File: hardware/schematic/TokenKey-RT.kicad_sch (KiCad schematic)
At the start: 0 parts

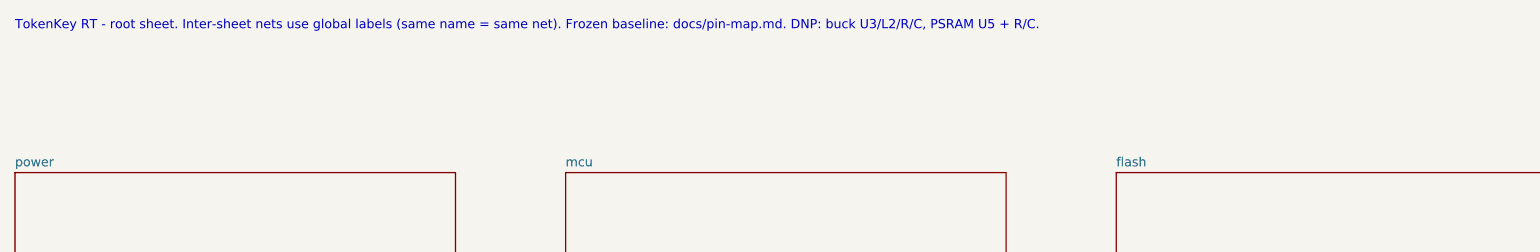
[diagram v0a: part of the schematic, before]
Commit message: PM review fixes: boot R_S, C51, decap note, notes, BOM fields
- MUST: add R22 (R_S) 1k 0402 0402WGF1001TCE / C11702 between Q1 drain
  (pin 3, new net BOOT_MODE0_Q) and BOOT_MODE0 (F11)
- C51 VBUS bulk 10uF 0603 -> 4.7uF 0402 (CL05A475MP5NRNC / C23733)
- docs/decisions.md: keep C11/C12; VDD_SOC total 32.5uF vs HDG ~33uF
- U3 description and root note: buck inductor is L1 (was "L2")
- mcu sheet note: WAKEUP (L6) / ONOFF (M6) rely on internal 100k PU
- APS6404L-3SQR-ZR pinout + USON-8 footprint checked vs AP Memory
  datasheet Rev 2.3 (no change); GPIO_SD_B0_04 ALT4 = FLEXSPIB_SS0_B
  confirmed in SDK fsl_iomuxc.h (H2 per DS Table 83)
- J3 TC2030 and TP1-TP5: MPN/LCSC "N/A - footprint only" + BOM_Note
- gen.py: reuse UUIDs from existing files (stable diffs), runs in-repo;
  netlist.json ignored
- kicad-cli sch erc: 0 errors, 0 warnings

Fixes #8
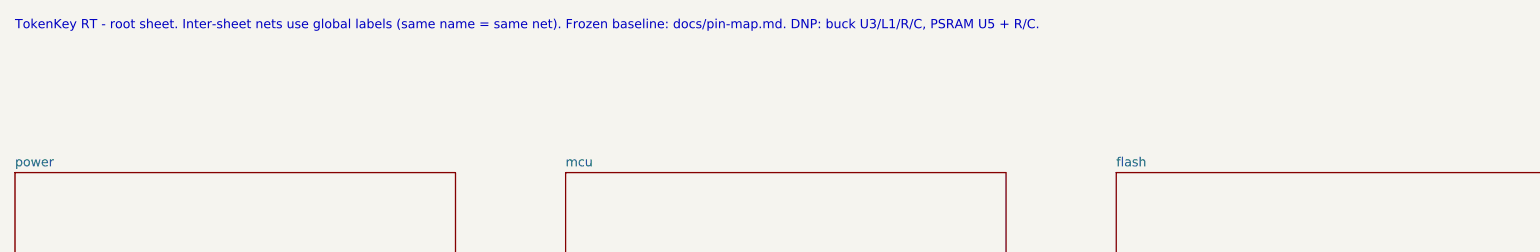
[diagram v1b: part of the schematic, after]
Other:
- note added: "TokenKey RT - root sheet. Inter-sheet nets use global labels (same name = same net). Frozen baseline: docs/pin-map.md. DNP: buck U3/L1/R/C, PSRAM U5 + R/C."
- note removed: "TokenKey RT - root sheet. Inter-sheet nets use global labels (same name = same net). Frozen baseline: docs/pin-map.md. DNP: buck U3/L2/R/C, PSRAM U5 + R/C."
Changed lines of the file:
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@@
 (kicad_sch (version 20250114) (generator "eeschema") (generator_version "9.0") (paper "A4") (title_block (title "TokenKey RT - i.MX RT1062 USB accessory") (rev "A0-draft") (company "TokenKey RT"))
-(text "TokenKey RT - root sheet. Inter-sheet nets use global labels (same name = same net). Frozen baseline: docs/pin-map.md. DNP: buck U3/L2/R/C, PSRAM U5 + R/C." (exclude_from_sim no) (at 30.48 20.32 0) (effects (font (size 1.27 1.27)) (justify left)))
+(text "TokenKey RT - root sheet. Inter-sheet nets use global labels (same name = same net). Frozen baseline: docs/pin-map.md. DNP: buck U3/L1/R/C, PSRAM U5 + R/C." (exclude_from_sim no) (at 30.48 20.32 0) (effects (font (size 1.27 1.27)) (justify left)))
 (sheet (at 30.48 40.64) (size 60.96 30.48) (exclude_from_sim no) (in_bom yes) (on_board yes) (dnp no) (fields_autoplaced yes) (stroke (width 0.1524) (type solid)) (fill (color 0 0 0 0.0000)) (property "Sheetname" "power" (at 30.48 39.93 0) (effects (font (size 1.27 1.27)) (justify left bottom))) (property "Sheetfile" "power.kicad_sch" (at 30.48 71.71 0) (effects (font (size 1.27 1.27)) (justify left top))) (instances (project "TokenKey-RT" (path "/69bcae8e-63e2-488c-b267-fe4af22cfb6e" (page "2")))))
 (sheet (at 106.68 40.64) (size 60.96 30.48) (exclude_from_sim no) (in_bom yes) (on_board yes) (dnp no) (fields_autoplaced yes) (stroke (width 0.1524) (type solid)) (fill (color 0 0 0 0.0000)) (property "Sheetname" "mcu" (at 106.68 39.93 0) (effects (font (size 1.27 1.27)) (justify left bottom))) (property "Sheetfile" "mcu.kicad_sch" (at 106.68 71.71 0) (effects (font (size 1.27 1.27)) (justify left top))) (instances (project "TokenKey-RT" (path "/69bcae8e-63e2-488c-b267-fe4af22cfb6e" (page "3")))))

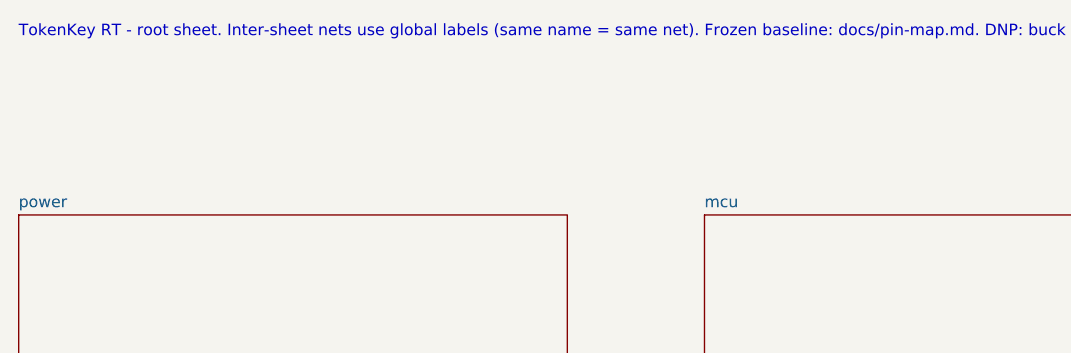
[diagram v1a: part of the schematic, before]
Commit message: Assembly note: bottom-side THT leads trimmed to <=1.5 mm after soldering
- Root sheet text note added via KiCad MCP add_schematic_text at (30.48, 25.4).
- docs/decisions.md row.
run_erc: 0 violations.

Fixes #37
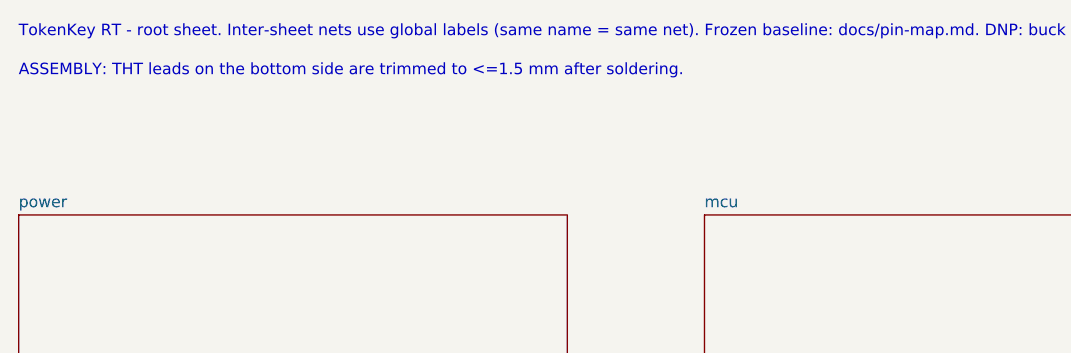
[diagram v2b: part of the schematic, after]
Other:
- note added: "ASSEMBLY: THT leads on the bottom side are trimmed to <=1.5 mm after soldering."
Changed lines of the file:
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@@
 (sheet (at 106.68 91.44) (size 60.96 30.48) (exclude_from_sim no) (in_bom yes) (on_board yes) (dnp no) (fields_autoplaced yes) (stroke (width 0.1524) (type solid)) (fill (color 0 0 0 0.0000)) (property "Sheetname" "ui" (at 106.68 90.73 0) (effects (font (size 1.27 1.27)) (justify left bottom))) (property "Sheetfile" "ui.kicad_sch" (at 106.68 122.51 0) (effects (font (size 1.27 1.27)) (justify left top))) (instances (project "TokenKey-RT" (path "/69bcae8e-63e2-488c-b267-fe4af22cfb6e" (page "6")))))
 (sheet (at 182.88 91.44) (size 60.96 30.48) (exclude_from_sim no) (in_bom yes) (on_board yes) (dnp no) (fields_autoplaced yes) (stroke (width 0.1524) (type solid)) (fill (color 0 0 0 0.0000)) (property "Sheetname" "debug" (at 182.88 90.73 0) (effects (font (size 1.27 1.27)) (justify left bottom))) (property "Sheetfile" "debug.kicad_sch" (at 182.88 122.51 0) (effects (font (size 1.27 1.27)) (justify left top))) (instances (project "TokenKey-RT" (path "/69bcae8e-63e2-488c-b267-fe4af22cfb6e" (page "7")))))
+	(text "ASSEMBLY: THT leads on the bottom side are trimmed to <=1.5 mm after soldering."
+		(exclude_from_sim no)
+		(at 30.48 25.4 0)
+		(effects
+			(font
+				(size 1.27 1.27)
+			)
+			(justify left bottom)
+		)
+	)
 (sheet_instances (path "/" (page "1")))
 (embedded_fonts no)
